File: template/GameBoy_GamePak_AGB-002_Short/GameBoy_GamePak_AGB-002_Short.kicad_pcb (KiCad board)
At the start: 2 copper layers, 51 x 25.9 mm, 1 part, among them J1 GameBoy_GamePak_AGB-002

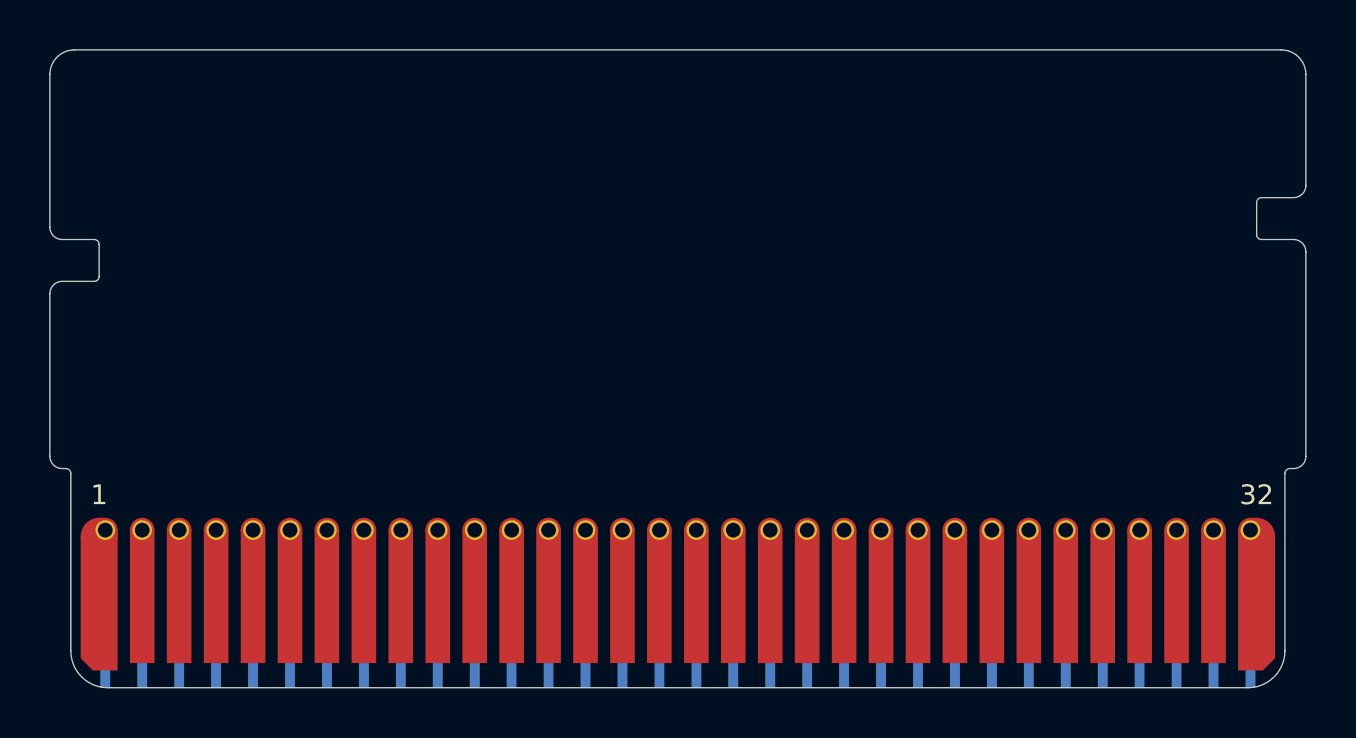
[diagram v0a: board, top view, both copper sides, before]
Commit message: Update all files to KiCAD 6.x format
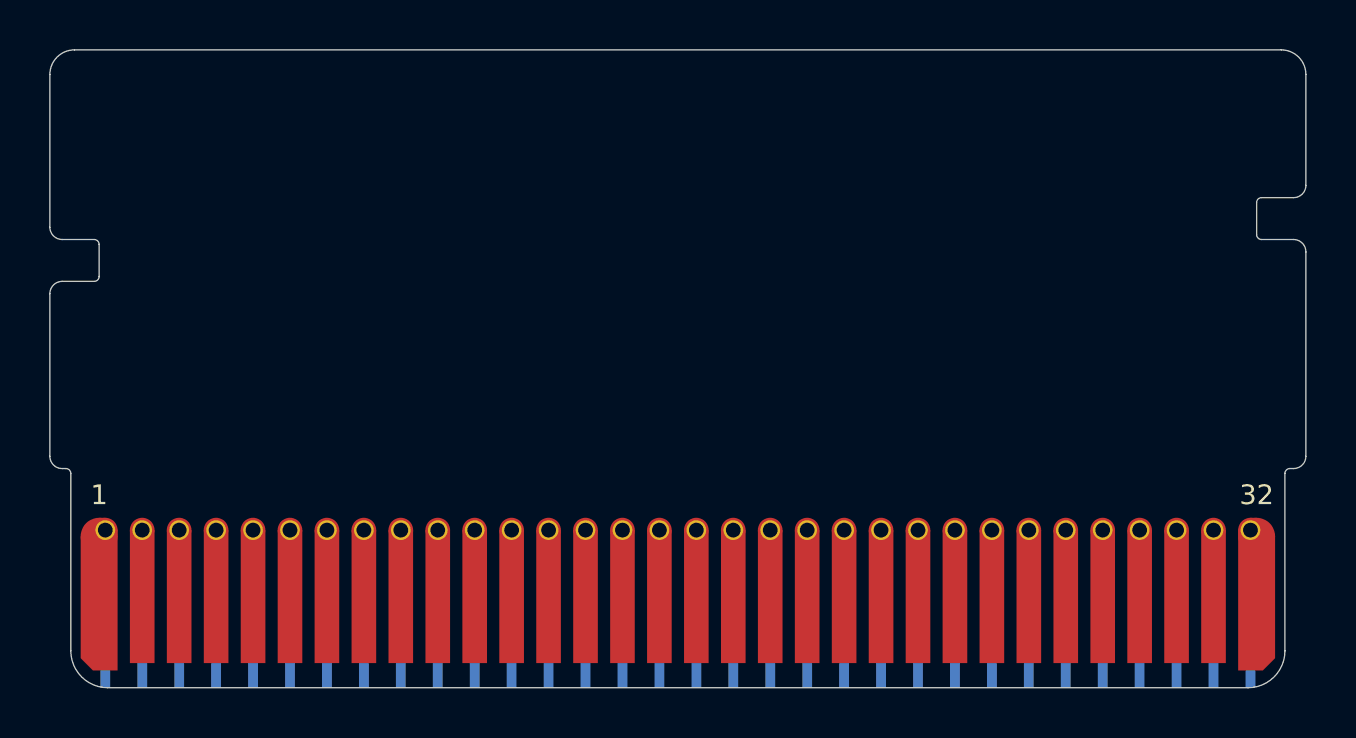
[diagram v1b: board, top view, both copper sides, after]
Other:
- outline, holes or cut-outs redrawn
- net class Default removed
